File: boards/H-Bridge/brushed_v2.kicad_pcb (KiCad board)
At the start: 2 copper layers, 53 parts, among them IC1 ISO1042QDWVQ1, IC2 MIC4606-1YML-TR, IC3 AD8410AWBRZ-RL, IC4 TC1108-3.3VDBTR, J1 V+, J2 V-, J3 Motor-, J4 Motor+, J5 CANBus, J6 Encoder, J7 Prog_Header, J8 UART, J9 12V+, Q1 NTBLS4D0N15MC, Q2 NTBLS4D0N15MC, Q3 NTBLS4D0N15MC, Q4 NTBLS4D0N15MC, U1 STM32F103C8Tx, U2 LSF0102DCUR, U3 LSF0102DCUR

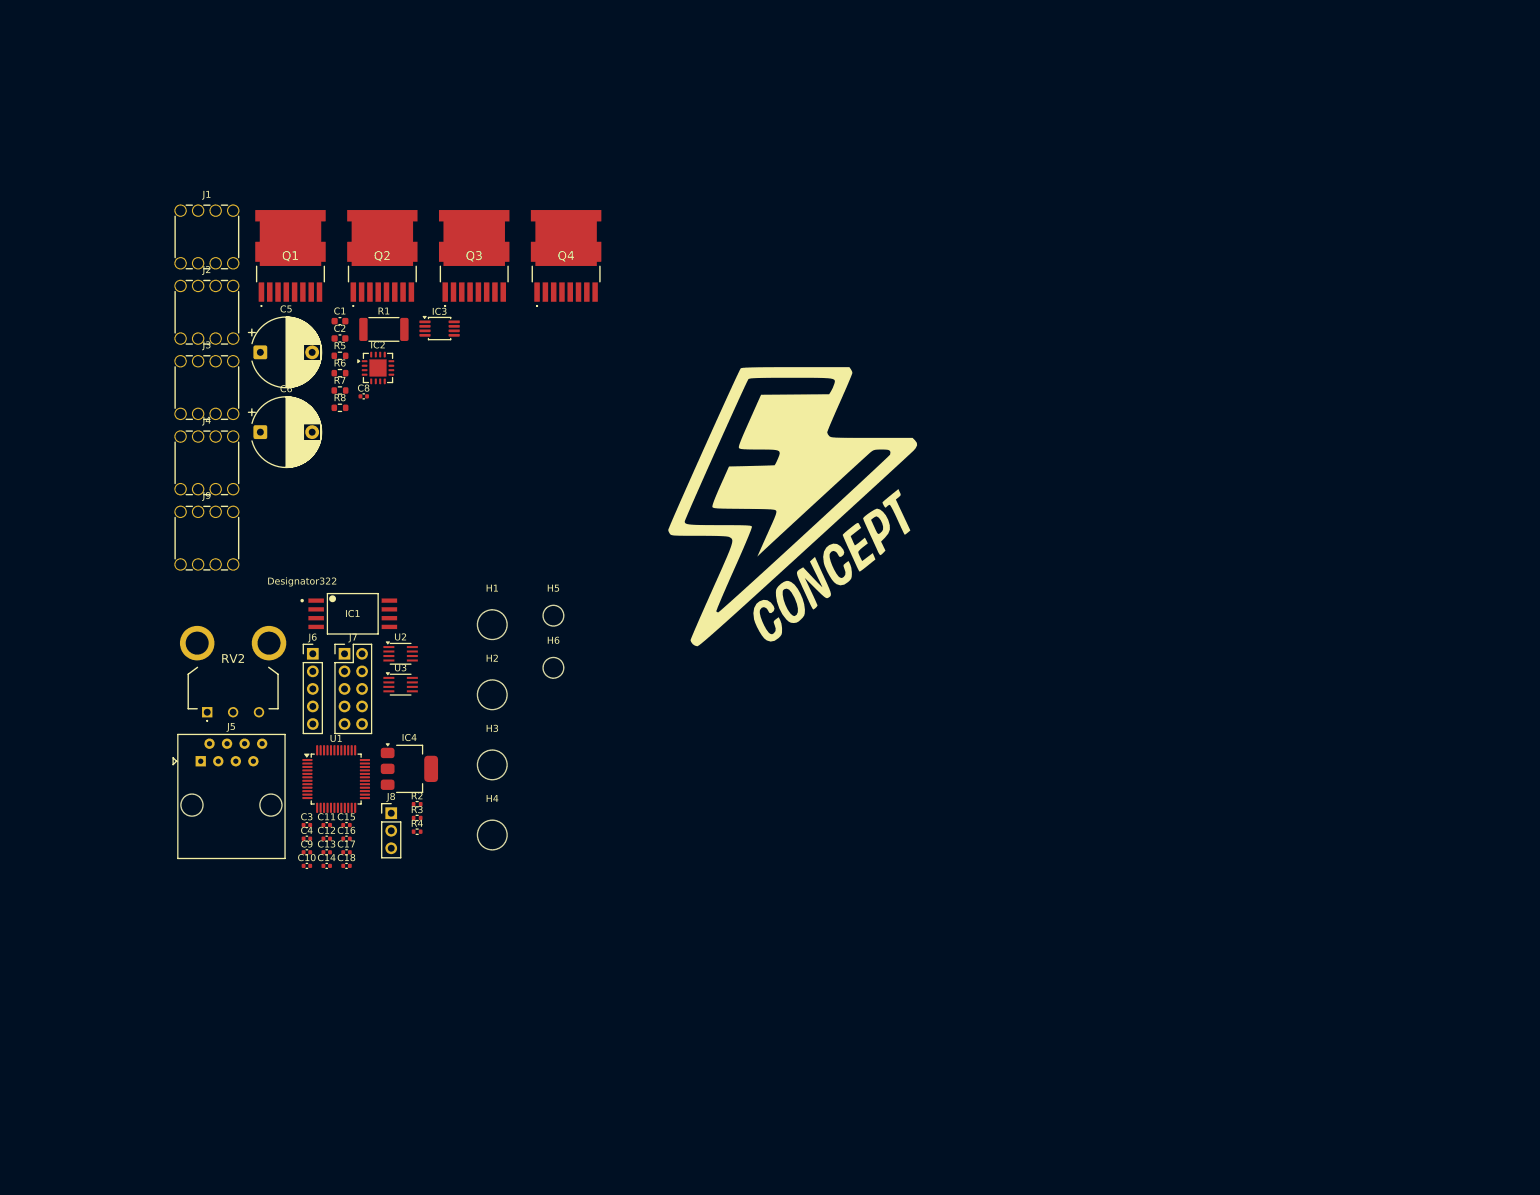
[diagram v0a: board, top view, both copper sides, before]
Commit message: started pcb layout, added small LEDs and SWO to schematic
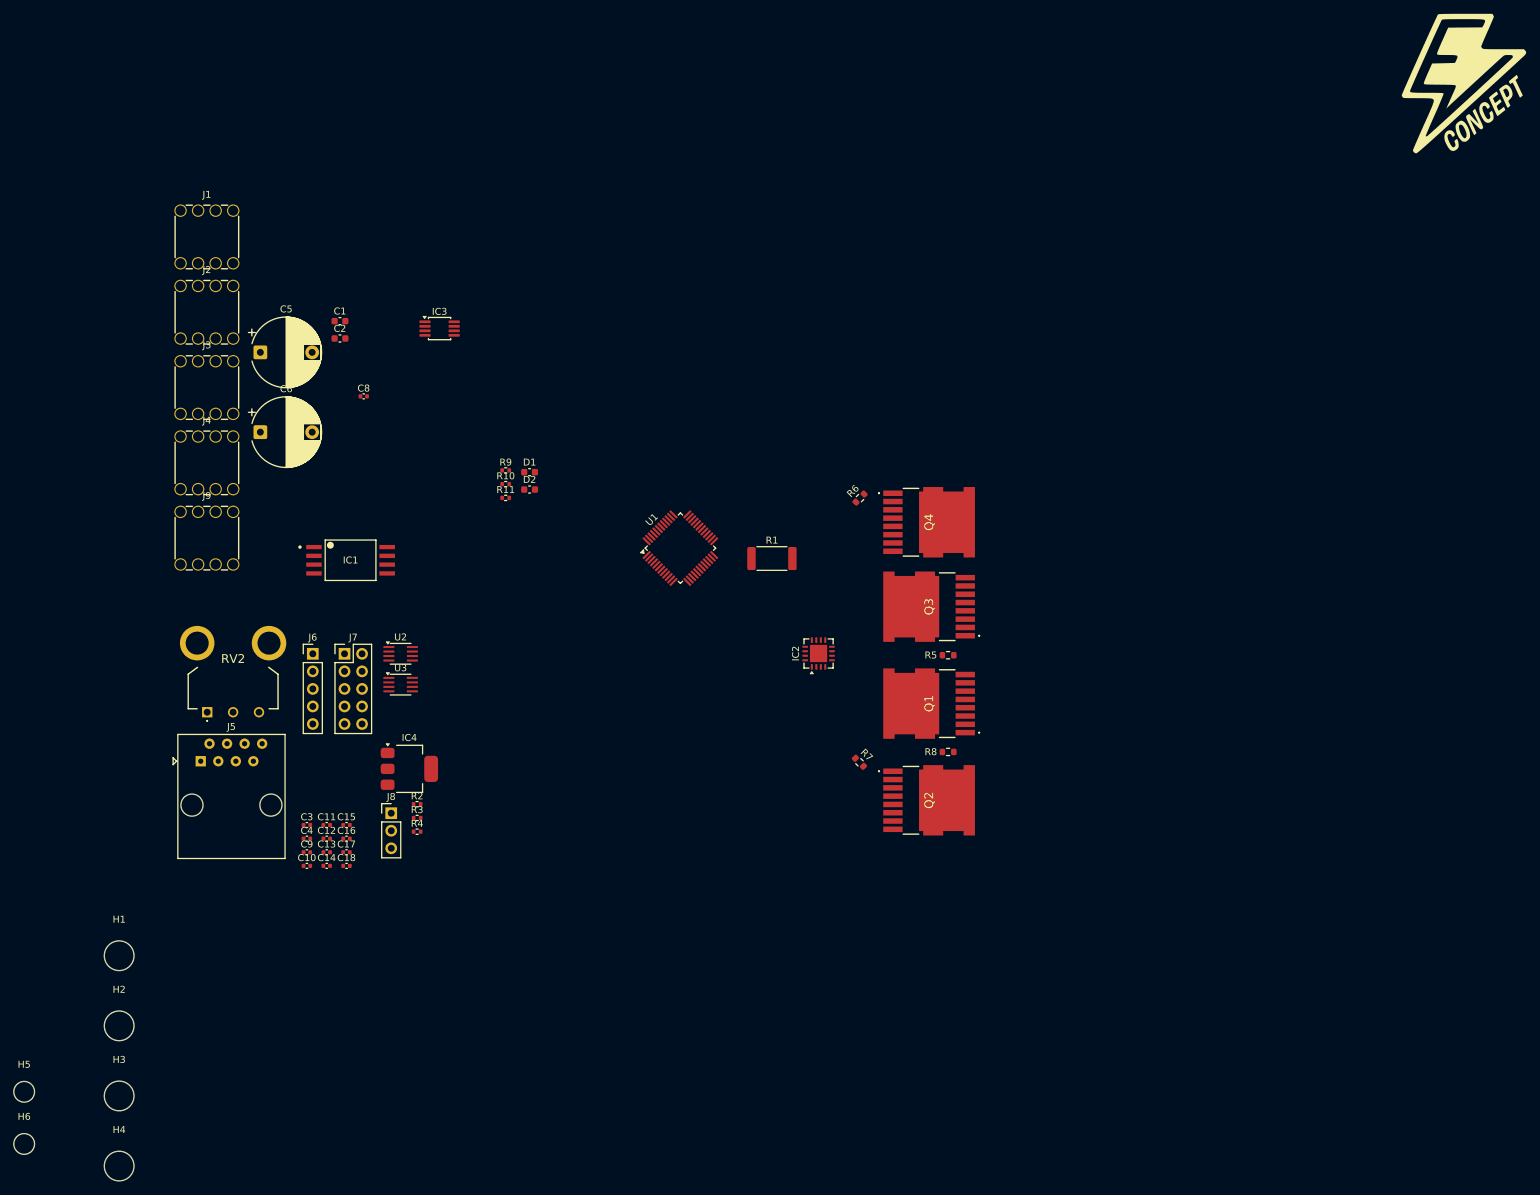
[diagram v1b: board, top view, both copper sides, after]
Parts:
- added D1: LED, Capacitor_SMD:C_0603_1608Metric, F.Cu at (129.4, 84.0)
- added D2: LED, Capacitor_SMD:C_0603_1608Metric, F.Cu at (129.4, 86.5)
- added R10: 1k, Resistor_SMD:R_0402_1005Metric, F.Cu at (126.0, 85.7)
- added R11: 1k, Resistor_SMD:R_0402_1005Metric, F.Cu at (126.0, 87.7)
- added R9: 10k, Resistor_SMD:R_0402_1005Metric, F.Cu at (126.0, 83.7)
- moved G*** 114.9 mm to (265.8, 27.8)
- moved Q1 112.9 mm to (187.2, 117.5), turned to 90 degrees
- moved Q2 111.7 mm to (187.2, 131.5), turned to -90 degrees
- moved H6 103.1 mm to (56.2, 181.2)
- moved H5 103.1 mm to (56.2, 173.7)
- moved R8 101.2 mm to (190.0, 124.5)
- moved R5 98.1 mm to (190.0, 110.5)
- moved R7 92.5 mm to (177.2, 126.0), turned to 135 degrees
- moved Q3 83.2 mm to (187.2, 103.5), turned to 90 degrees
- moved R6 77.4 mm to (177.2, 87.8), turned to 45 degrees
- moved IC2 76.0 mm to (171.2, 110.2), turned to 90 degrees
- moved H1 72.2 mm to (70.0, 154.0)
- moved H2 72.2 mm to (70.0, 164.2)
- moved H3 72.2 mm to (70.0, 174.3)
- moved H4 72.2 mm to (70.0, 184.4)
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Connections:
- J7 pad 5: unconnected-(J7-Pin_5-Pad5) -> /MCU&Low_Voltage/SWO
- RV2 pad 2: /MCU&Low_Voltage/Pot_In -> /MCU&Low_Voltage/POT_IN
- U1 pad 11: /MCU&Low_Voltage/SENSE -> /MCU&Low_Voltage/POT_IN
- U1 pad 17: unconnected-(U1-PA7-Pad17) -> /MCU&Low_Voltage/SENSE
- U1 pad 39: unconnected-(U1-PB3-Pad39) -> /MCU&Low_Voltage/SWO
- U1 pad 40: unconnected-(U1-PB4-Pad40) -> /MCU&Low_Voltage/LED_2
- U1 pad 41: unconnected-(U1-PB5-Pad41) -> /MCU&Low_Voltage/LED_1
- U1 pad 44: GND -> Net-(U1-BOOT0)
- U1 pad 7: GND -> +3.3V

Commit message: modified pwm signals to be on same timer
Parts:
- moved R1 38.9 mm to (202.2, 105.8), turned to 90 degrees
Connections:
- U1 pad 13: unconnected-(U1-PA3-Pad13) -> /MCU&Low_Voltage/SENSE
- U1 pad 16: unconnected-(U1-PA6-Pad16) -> /MCU&Low_Voltage/AHI
- U1 pad 17: /MCU&Low_Voltage/SENSE -> /MCU&Low_Voltage/ALI
- U1 pad 18: /MCU&Low_Voltage/AHI -> /MCU&Low_Voltage/BLI
- U1 pad 19: /MCU&Low_Voltage/ALI -> /MCU&Low_Voltage/BHI
- U1 pad 21: /MCU&Low_Voltage/BLI -> unconnected-(U1-PB10-Pad21)
- U1 pad 22: /MCU&Low_Voltage/BHI -> unconnected-(U1-PB11-Pad22)
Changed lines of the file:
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@@
 			(layers "F.Cu" "F.Mask" "F.Paste")
 			(roundrect_rratio 0.25)
-			(net "unconnected-(U1-PA3-Pad13)")
+			(net "/MCU&Low_Voltage/SENSE")
 			(pinfunction "PA3_13")
-			(pintype "bidirectional+no_connect")
+			(pintype "bidirectional")
 		)
 		(pad "14" smd roundrect
@@
 			(layers "F.Cu" "F.Mask" "F.Paste")
 			(roundrect_rratio 0.25)
-			(net "unconnected-(U1-PA6-Pad16)")
+			(net "/MCU&Low_Voltage/AHI")
 			(pinfunction "PA6_16")
-			(pintype "bidirectional+no_connect")
+			(pintype "bidirectional")
 		)
 		(pad "17" smd roundrect
@@
 			(layers "F.Cu" "F.Mask" "F.Paste")
 			(roundrect_rratio 0.25)
-			(net "/MCU&Low_Voltage/SENSE")
+			(net "/MCU&Low_Voltage/ALI")
 			(pinfunction "PA7_17")
 			(pintype "bidirectional")
@@
 			(layers "F.Cu" "F.Mask" "F.Paste")
 			(roundrect_rratio 0.25)
-			(net "/MCU&Low_Voltage/AHI")
+			(net "/MCU&Low_Voltage/BLI")
 			(pinfunction "PB0_18")
 			(pintype "bidirectional")
@@
 			(layers "F.Cu" "F.Mask" "F.Paste")
 			(roundrect_rratio 0.25)
-			(net "/MCU&Low_Voltage/ALI")
+			(net "/MCU&Low_Voltage/BHI")
 			(pinfunction "PB1_19")
 			(pintype "bidirectional")
@@
 			(layers "F.Cu" "F.Mask" "F.Paste")
 			(roundrect_rratio 0.25)
-			(net "/MCU&Low_Voltage/BLI")
+			(net "unconnected-(U1-PB10-Pad21)")
 			(pinfunction "PB10_21")
-			(pintype "bidirectional")
+			(pintype "bidirectional+no_connect")
 		)
 		(pad "22" smd roundrect
@@
 			(layers "F.Cu" "F.Mask" "F.Paste")
 			(roundrect_rratio 0.25)
-			(net "/MCU&Low_Voltage/BHI")
+			(net "unconnected-(U1-PB11-Pad22)")
 			(pinfunction "PB11_22")
-			(pintype "bidirectional")
+			(pintype "bidirectional+no_connect")
 		)
 		(pad "23" smd roundrect
@@
 	(footprint "Resistor_SMD:R_2512_6332Metric"
 		(layer "F.Cu")
-		(at 164.5 96.5)
+		(at 202.25 105.75 90)
 		(descr "Resistor SMD 2512 (6332 Metric), square (rectangular) end terminal, IPC-7351 nominal, (Body size source: IPC-SM-782 page 72, https://www.pcb-3d.com/wordpress/wp-content/uploads/ipc-sm-782a_amendment_1_and_2.pdf)")
 		(tags "resistor")
 		(property "Reference" "R1"
-			(at 0 -2.63 0)
+			(at 0 -2.63 90)
 			(layer "F.SilkS")
 			(effects
@@
 		)
 		(property "Value" ".001"
-			(at 0 2.63 0)
+			(at 0 2.63 90)
 			(layer "F.Fab")
 			(effects
@@
 		)
 		(property "Datasheet" ""
-			(at 0 0 0)
+			(at 0 0 90)
 			(layer "F.Fab")
 			(hide yes)
@@
 		)
 		(property "Description" "Resistor, US symbol, CSS2H-2512R-1L00FE"
-			(at 0 0 0)
+			(at 0 0 90)
 			(layer "F.Fab")
 			(hide yes)
@@
 		)
 		(property "KiLib_Generator" "SMD_2terminal_chip_molded"
-			(at 0 0 0)
+			(at 0 0 90)
 			(layer "F.SilkS")
 			(hide yes)
@@
 		)
 		(fp_text user "${REFERENCE}"
-			(at 0 0 0)
+			(at 0 0 90)
 			(layer "F.Fab")
 			(effects
@@
 		)
 		(pad "1" smd roundrect
-			(at -2.9625 0)
+			(at -2.9625 0 90)
 			(size 1.225 3.35)
 			(layers "F.Cu" "F.Mask" "F.Paste")
@@
 		)
 		(pad "2" smd roundrect
-			(at 2.9625 0)
+			(at 2.9625 0 90)
 			(size 1.225 3.35)
 			(layers "F.Cu" "F.Mask" "F.Paste")

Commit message: did some layout
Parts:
- moved J4 145.8 mm to (224.5, 116.8)
- moved J3 144.6 mm to (224.2, 101.2)
- moved R6 30.1 mm to (207.2, 85.2), turned to -45 degrees
- moved R7 20.3 mm to (196.2, 133.0)
- moved Q4 18.2 mm to (204.8, 96.0), turned to 180 degrees
- moved Q2 17.8 mm to (204.6, 127.2), turned to 0 degrees
- moved R1 13.3 mm to (212.2, 114.5), turned to 0 degrees
- moved Q3 3.78 mm to (190.3, 101.3)
- moved Q1 3.47 mm to (190.2, 115.8)
- moved R5 2.66 mm to (191.8, 108.5)
- moved R8 2.25 mm to (191.7, 123.0)
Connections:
- IC3 pad 1: /High Voltage&Sense/BHS -> /High Voltage&Sense/SHUNT-
- IC3 pad 8: /High Voltage&Sense/SHUNT+ -> /High Voltage&Sense/AHS
- J4 pad 1: /High Voltage&Sense/AHS -> /High Voltage&Sense/SHUNT-
- R1 pad 1: /High Voltage&Sense/SHUNT+ -> /High Voltage&Sense/AHS
- R1 pad 2: /High Voltage&Sense/BHS -> /High Voltage&Sense/SHUNT-

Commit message: thought some more
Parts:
- moved J3 1.75 mm to (226.0, 101.2)
- moved J4 1.35 mm to (225.8, 116.2)
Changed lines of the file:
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@@
 	(footprint "ThreadedConnector:WP-BUTR_7460307"
 		(layer "F.Cu")
-		(at 224.5 116.75)
+		(at 225.75 116.25)
 		(property "Reference" "J4"
 			(at 0 -6.135 0)
@@
 	(footprint "ThreadedConnector:WP-BUTR_7460307"
 		(layer "F.Cu")
-		(at 224.25 101.25)
+		(at 226 101.25)
 		(property "Reference" "J3"
 			(at 0 -6.135 0)

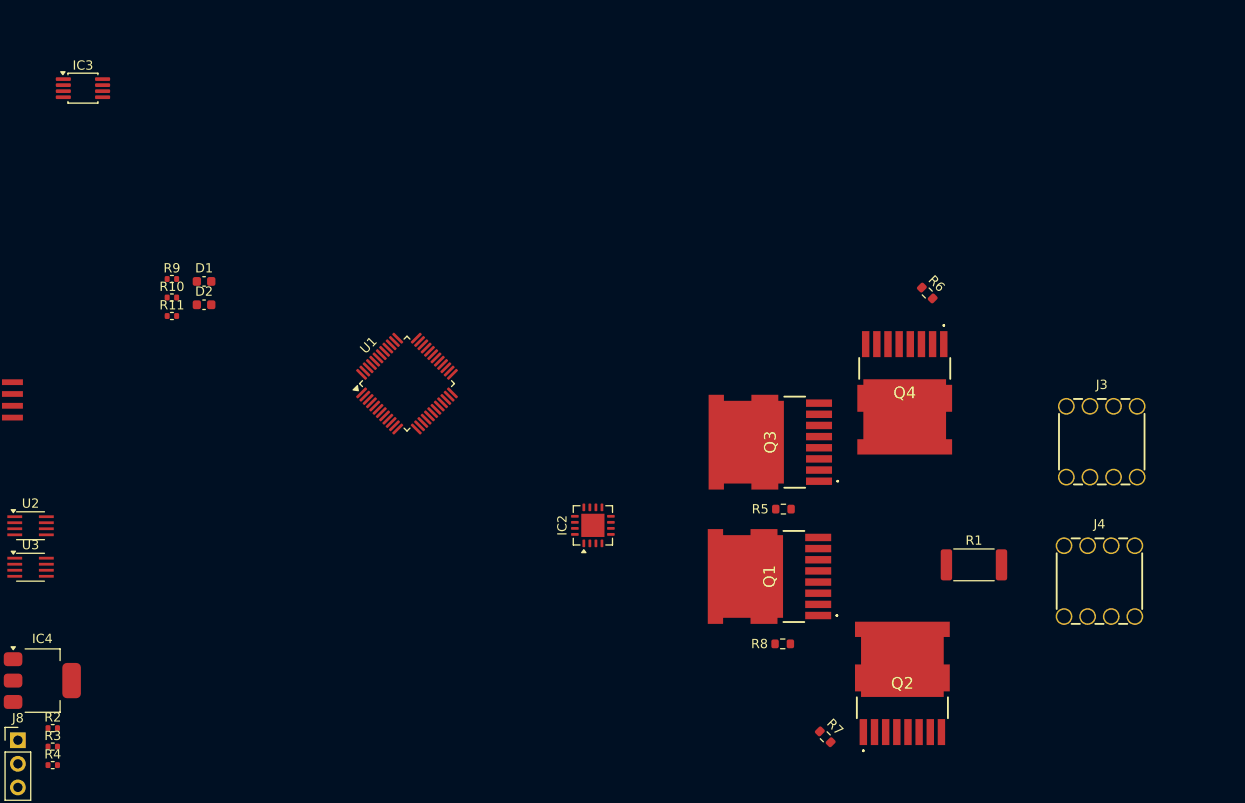
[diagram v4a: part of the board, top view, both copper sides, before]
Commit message: added negative voltage per h-bridge docs
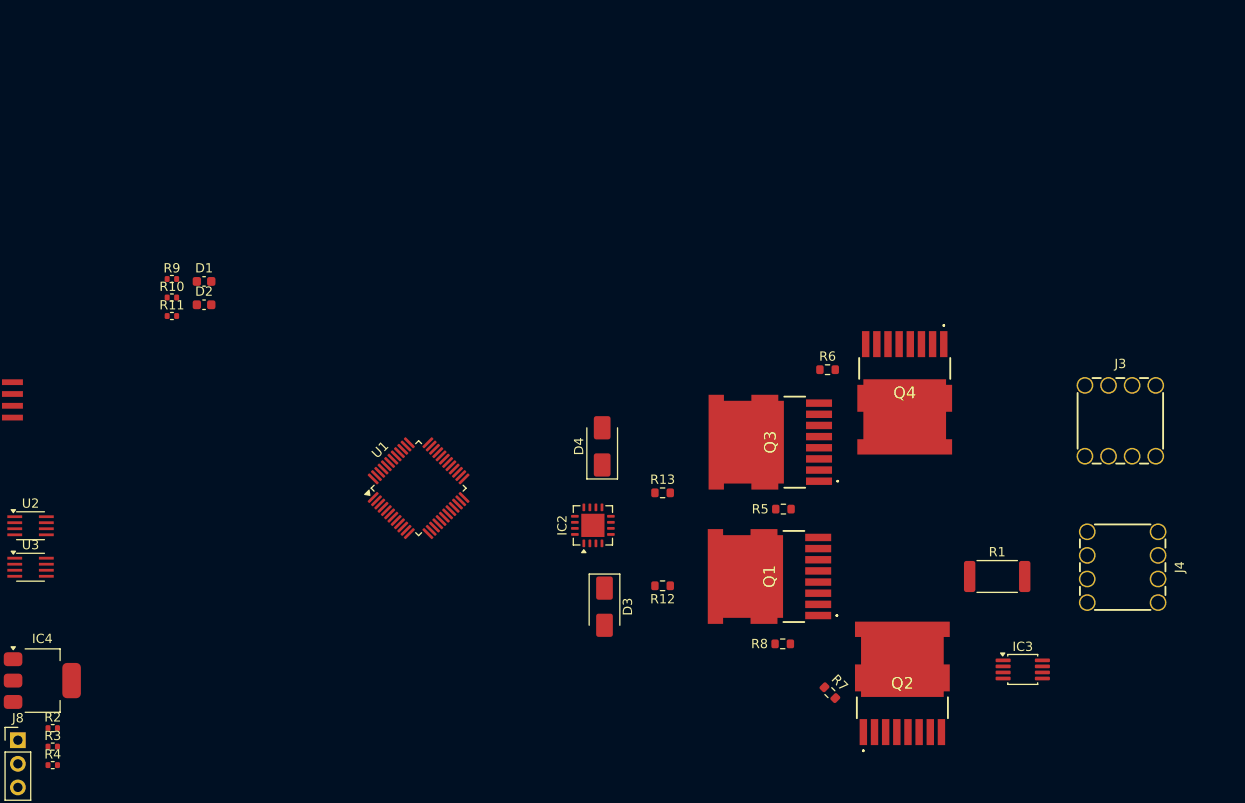
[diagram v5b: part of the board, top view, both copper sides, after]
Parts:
- added D3: SS1200, Diode_SMD:D_SMA, F.Cu at (172.5, 119.0)
- added D4: SS1200, Diode_SMD:D_SMA, F.Cu at (172.2, 101.8)
- added R12: 3, Resistor_SMD:R_0603_1608Metric, F.Cu at (178.8, 116.8)
- added R13: 3, Resistor_SMD:R_0603_1608Metric, F.Cu at (178.8, 106.8)
- moved IC3 118.9 mm to (217.5, 125.8)
- moved R6 13.5 mm to (196.5, 93.5), turned to 0 degrees
- moved U1 11.3 mm to (152.5, 106.2)
- moved R7 4.78 mm to (196.8, 128.2)
- moved J3 3.01 mm to (228.0, 99.0)
- moved J4 2.92 mm to (228.2, 114.8), turned to -90 degrees
- moved R1 2.80 mm to (214.8, 115.8)
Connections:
- IC3 pad 8: /High Voltage&Sense/AHS -> /High Voltage&Sense/SHUNT+
- J3 pad 1: /High Voltage&Sense/BHS -> Net-(J3-Pin_1)
- J4 pad 1: /High Voltage&Sense/SHUNT- -> /High Voltage&Sense/SHUNT+
- Q1 pad 1: /High Voltage&Sense/AHS -> /High Voltage&Sense/SHUNT-
- Q1 pad 2: /High Voltage&Sense/AHS -> /High Voltage&Sense/SHUNT-
- Q1 pad 3: /High Voltage&Sense/AHS -> /High Voltage&Sense/SHUNT-
- Q1 pad 4: /High Voltage&Sense/AHS -> /High Voltage&Sense/SHUNT-
- Q1 pad 5: /High Voltage&Sense/AHS -> /High Voltage&Sense/SHUNT-
- Q1 pad 6: /High Voltage&Sense/AHS -> /High Voltage&Sense/SHUNT-
- Q1 pad 7: /High Voltage&Sense/AHS -> /High Voltage&Sense/SHUNT-
- Q2 pad 10: /High Voltage&Sense/AHS -> /High Voltage&Sense/SHUNT-
- Q2 pad 11: /High Voltage&Sense/AHS -> /High Voltage&Sense/SHUNT-
- Q2 pad 12: /High Voltage&Sense/AHS -> /High Voltage&Sense/SHUNT-
- Q2 pad 13: /High Voltage&Sense/AHS -> /High Voltage&Sense/SHUNT-
- Q2 pad 9: /High Voltage&Sense/AHS -> /High Voltage&Sense/SHUNT-
- Q3 pad 1: /High Voltage&Sense/BHS -> Net-(J3-Pin_1)
- Q3 pad 2: /High Voltage&Sense/BHS -> Net-(J3-Pin_1)
- Q3 pad 3: /High Voltage&Sense/BHS -> Net-(J3-Pin_1)
- Q3 pad 4: /High Voltage&Sense/BHS -> Net-(J3-Pin_1)
- Q3 pad 5: /High Voltage&Sense/BHS -> Net-(J3-Pin_1)
- Q3 pad 6: /High Voltage&Sense/BHS -> Net-(J3-Pin_1)
- Q3 pad 7: /High Voltage&Sense/BHS -> Net-(J3-Pin_1)
- Q4 pad 10: /High Voltage&Sense/BHS -> Net-(J3-Pin_1)
- Q4 pad 11: /High Voltage&Sense/BHS -> Net-(J3-Pin_1)
- Q4 pad 12: /High Voltage&Sense/BHS -> Net-(J3-Pin_1)
- Q4 pad 13: /High Voltage&Sense/BHS -> Net-(J3-Pin_1)
- Q4 pad 9: /High Voltage&Sense/BHS -> Net-(J3-Pin_1)
- R1 pad 1: /High Voltage&Sense/AHS -> /High Voltage&Sense/SHUNT-
- R1 pad 2: /High Voltage&Sense/SHUNT- -> /High Voltage&Sense/SHUNT+
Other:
- copper layers 2 -> 4
